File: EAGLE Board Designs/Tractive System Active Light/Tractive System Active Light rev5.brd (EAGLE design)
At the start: 67.5 x 23.1 mm, 13 parts, among them J1 CONNECTOR-4_μF_S_RA_

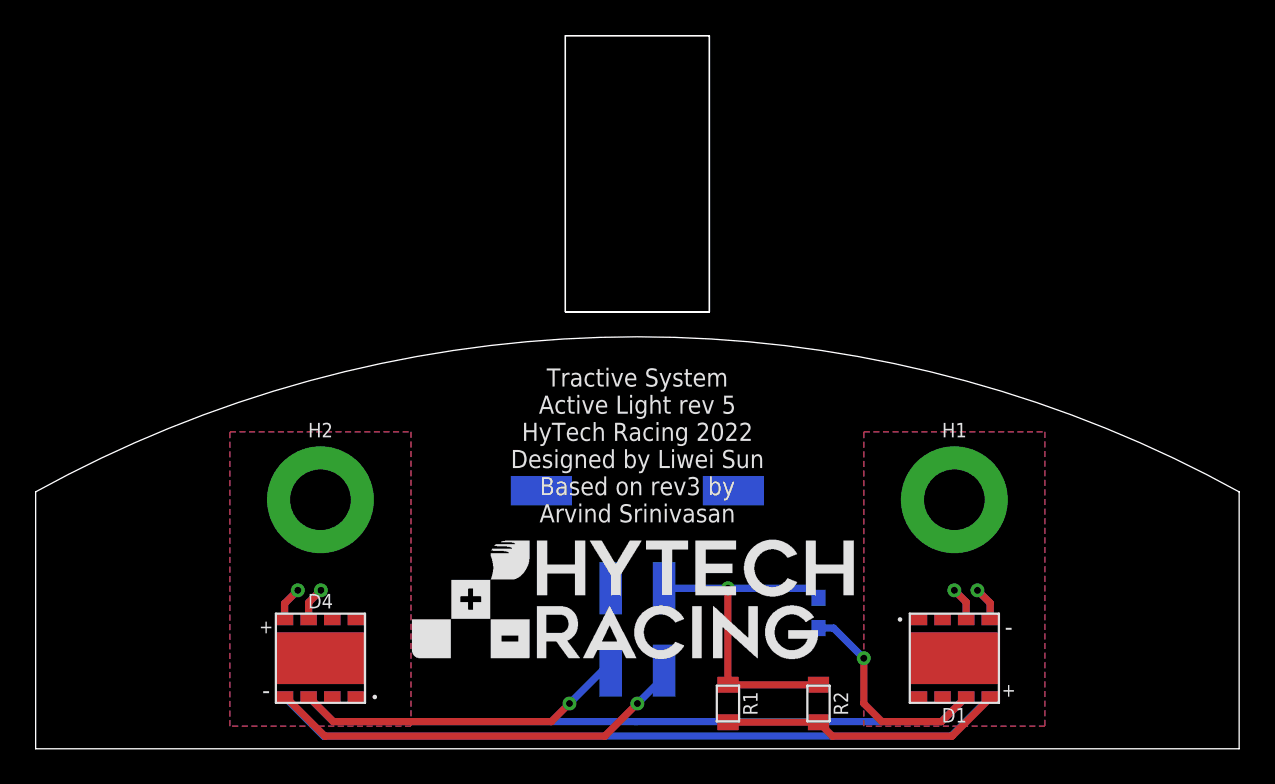
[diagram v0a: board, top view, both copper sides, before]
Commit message: Moved board dimensions
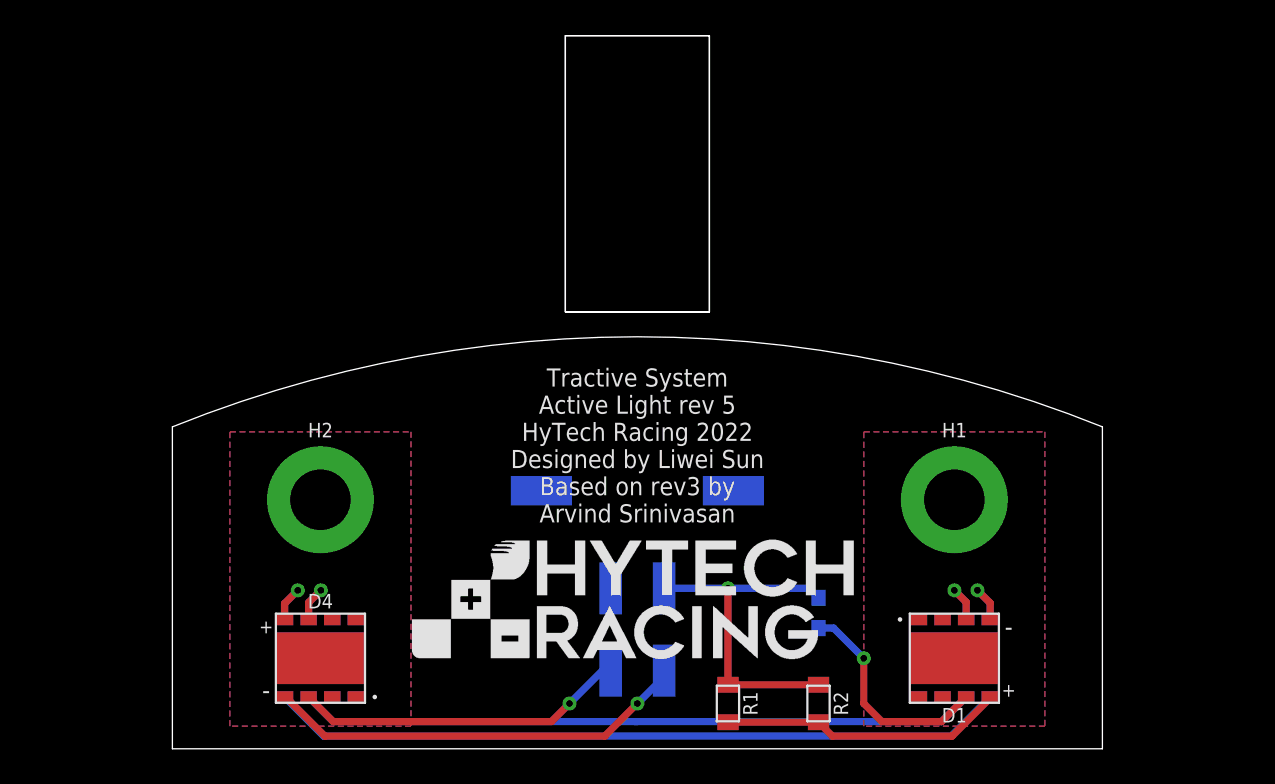
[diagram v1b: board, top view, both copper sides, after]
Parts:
- removed U$1: (no value), HyTechManufacturing:LOGO_HYTECH_SQUARE_EXTRA_LARGE
- removed U$3: (no value), HyTechManufacturing:LOGO_GT_MEDIUM
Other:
- board size 67.5 x 23.1 mm -> 52.2 x 23.1 mm
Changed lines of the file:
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@@
 <board>
 <plain>
-<wire x1="33.7566" y1="0" x2="-33.7566" y2="0" width="0" layer="20"/>
-<wire x1="33.7566" y1="0" x2="33.7566" y2="14.412834375" width="0" layer="20"/>
-<wire x1="-33.7566" y1="0" x2="-33.7566" y2="14.412834375" width="0" layer="20"/>
-<wire x1="33.7566" y1="14.412834375" x2="-33.7566" y2="14.412834375" width="0" layer="20" curve="57.798736"/>
+<wire x1="26.0858" y1="0" x2="26.0858" y2="18.0594" width="0" layer="20"/>
+<wire x1="-26.0858" y1="0" x2="-26.0858" y2="18.0594" width="0" layer="20"/>
 <text x="0" y="12.7" size="1.016" layer="21" align="bottom-center">Tractive System
 Active Light rev 5
@@
 Based on rev3 by
 Arvind Srinivasan</text>
+<wire x1="26.0858" y1="0" x2="-26.0858" y2="0" width="0" layer="20"/>
+<wire x1="26.0858" y1="18.0594" x2="-26.0858" y2="18.0594" width="0" layer="20" curve="43.850961"/>
 </plain>
 <attributes>
@@
 <attribute name="NAME" x="-17.78" y="7.874" size="0.8128" layer="25" font="vector" align="bottom-center"/>
 </element>
-<element name="U$1" library="HyTechManufacturing" package="LOGO_HYTECH_SQUARE_EXTRA_LARGE" value="" x="-25.4" y="7.62" smashed="yes" rot="MR0"/>
-<element name="U$3" library="HyTechManufacturing" package="LOGO_GT_MEDIUM" value="" x="26.67" y="7.62" smashed="yes" rot="MR0"/>
 <element name="U$2" library="HyTechManufacturing" package="LOGO_HYTECH_MEDIUM" value="" x="-12.7" y="5.08" smashed="yes"/>
 </elements>

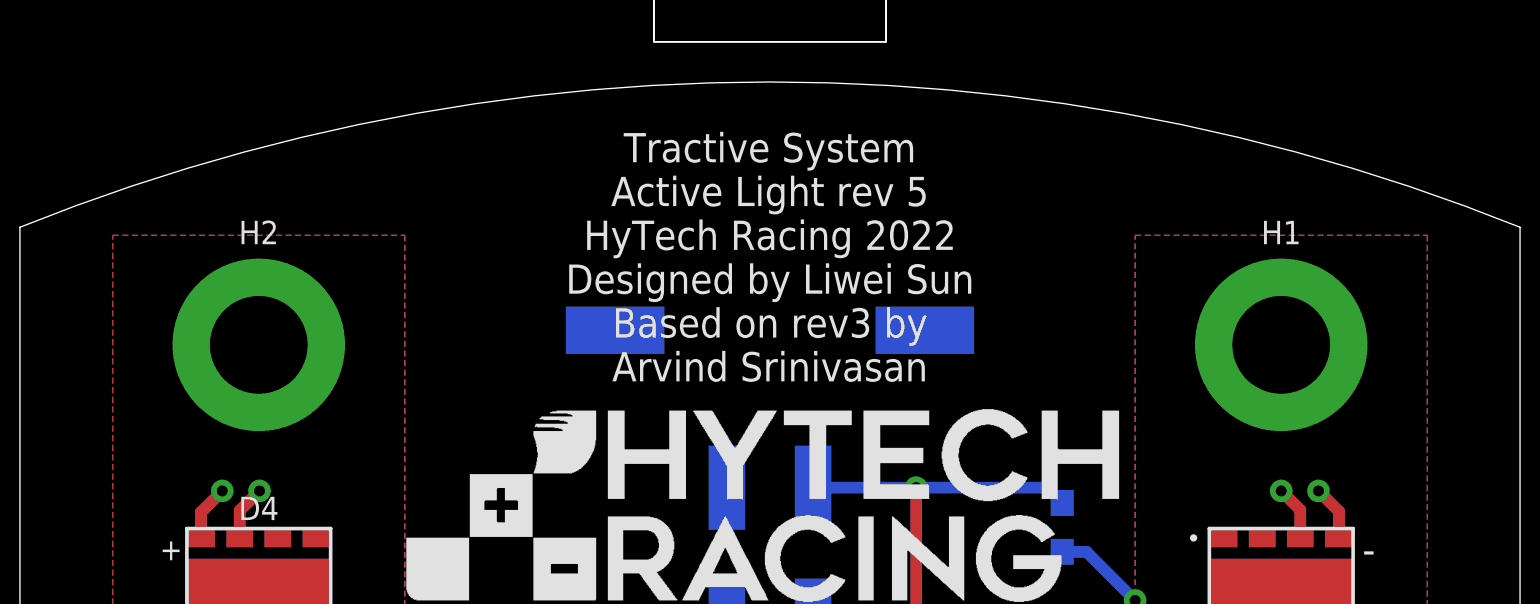
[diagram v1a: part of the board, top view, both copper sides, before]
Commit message: move mounting holes 50 mils higher
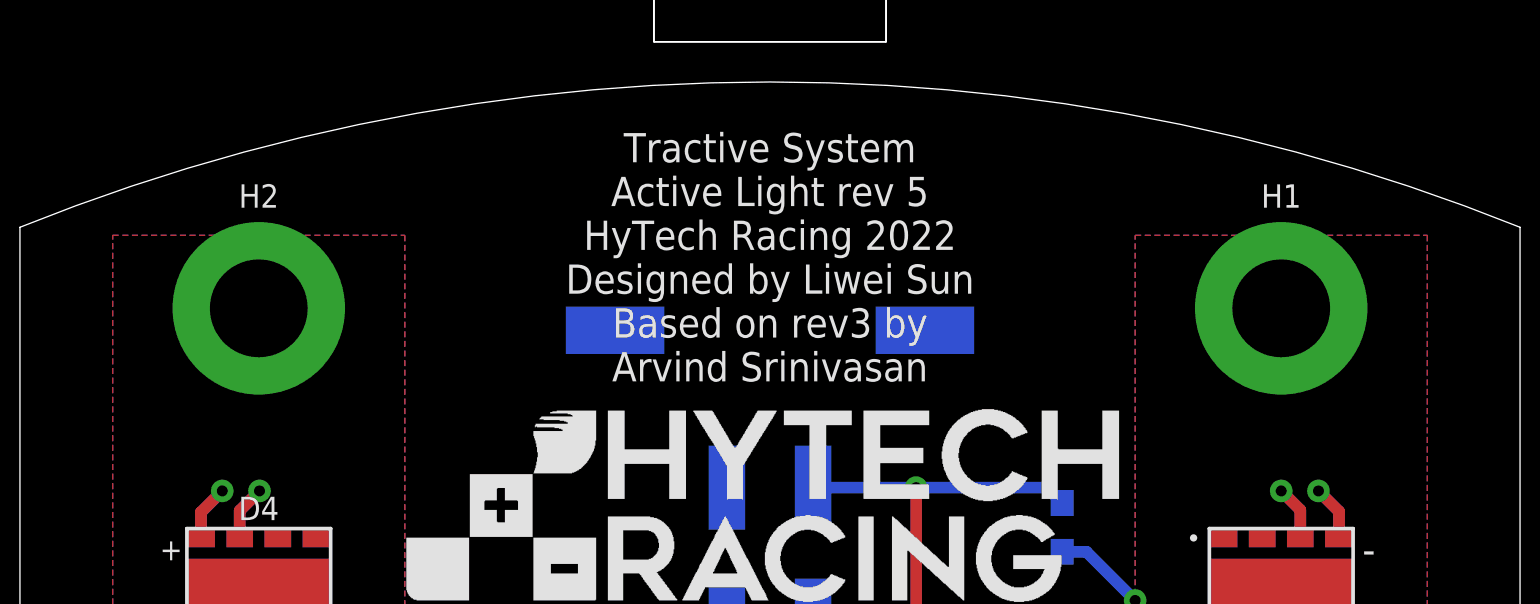
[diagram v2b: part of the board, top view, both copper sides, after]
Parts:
- moved H1 1.27 mm to (17.8, 15.2)
- moved H2 1.27 mm to (-17.8, 15.2)
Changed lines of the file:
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@@
 <attribute name="NAME" x="0" y="0.127" size="0.8128" layer="26" rot="MR0" align="bottom-center"/>
 </element>
-<element name="H1" library="HyTechDevices" package="MOUNTING_M3" value="MOUNTING_HEATSINK_M3" x="17.78" y="13.97" smashed="yes">
-<attribute name="NAME" x="17.78" y="17.47" size="0.8128" layer="25" font="vector" align="bottom-center"/>
+<element name="H1" library="HyTechDevices" package="MOUNTING_M3" value="MOUNTING_HEATSINK_M3" x="17.78" y="15.24" smashed="yes">
+<attribute name="NAME" x="17.78" y="18.74" size="0.8128" layer="25" font="vector" align="bottom-center"/>
 </element>
-<element name="H2" library="HyTechDevices" package="MOUNTING_M3" value="MOUNTING_HEATSINK_M3" x="-17.78" y="13.97" smashed="yes">
-<attribute name="NAME" x="-17.78" y="17.47" size="0.8128" layer="25" font="vector" align="bottom-center"/>
+<element name="H2" library="HyTechDevices" package="MOUNTING_M3" value="MOUNTING_HEATSINK_M3" x="-17.78" y="15.24" smashed="yes">
+<attribute name="NAME" x="-17.78" y="18.74" size="0.8128" layer="25" font="vector" align="bottom-center"/>
 </element>
 <element name="D1" library="HyTechDevices" package="IN-505FCHWV" value="LED_RGBW_IN-505FCHWV" x="17.78" y="5.08" smashed="yes" rot="R180">
